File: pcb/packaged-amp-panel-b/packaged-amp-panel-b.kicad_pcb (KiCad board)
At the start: 2 copper layers, 70.9 x 24.2 mm, 0 parts

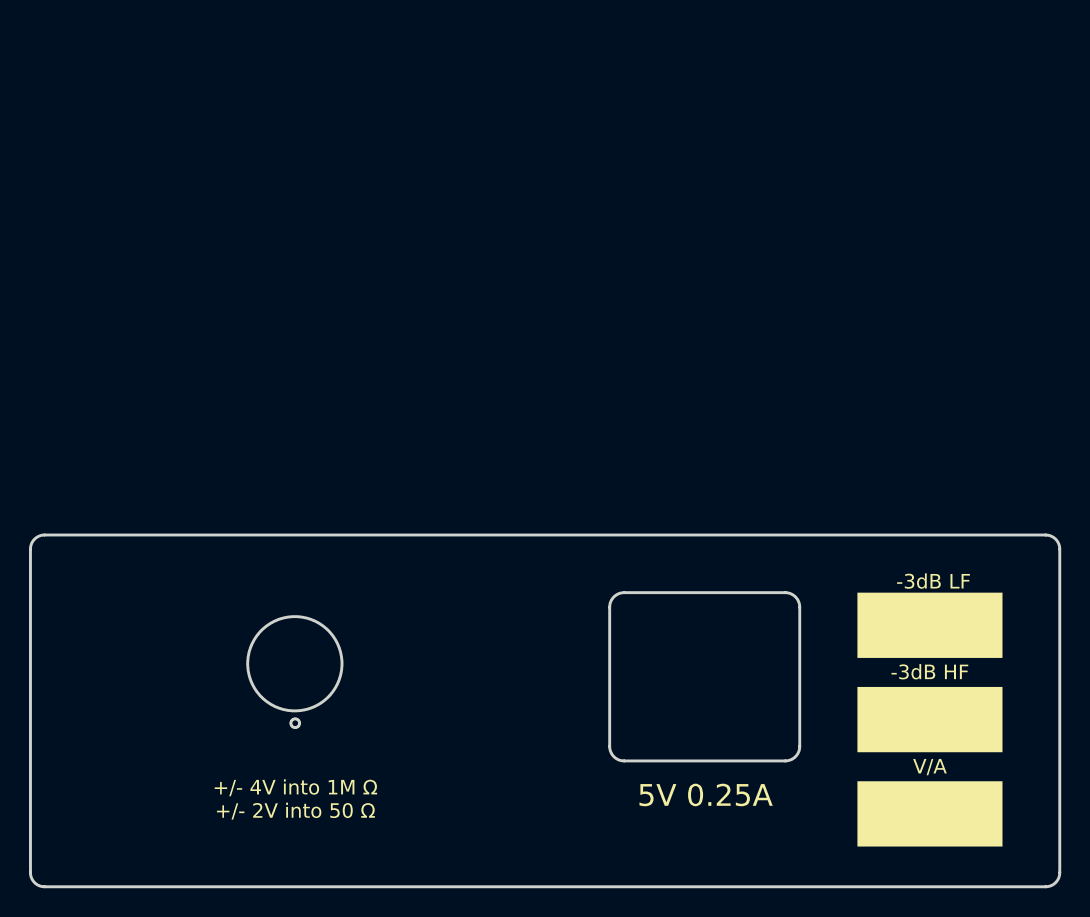
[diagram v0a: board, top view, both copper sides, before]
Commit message: updated panels
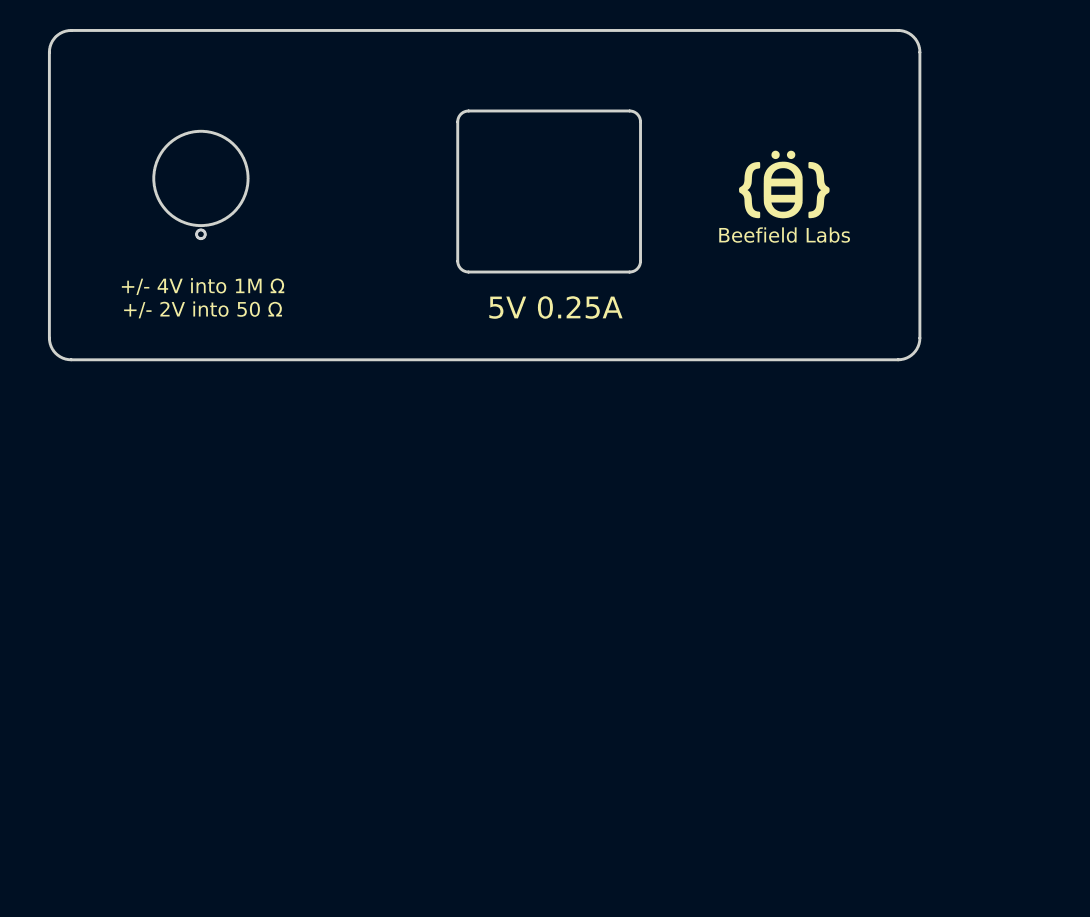
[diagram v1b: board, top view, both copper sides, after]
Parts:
- added G***: LOGO, wbraun_smd:beefield_logo_small, F.Cu at (144.7, 69.8)
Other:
- board size 70.9 x 24.2 mm -> 60 x 22.7 mm
- board text added: "Beefield Labs"
- board text removed: "-3dB HF"
- board text removed: "-3dB LF"
- board text removed: "V/A"

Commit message: next revision
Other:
- outline, holes or cut-outs redrawn
- board text added: "+/- 4V into 1M Ω"
- board text added: "5V 0.4A"
- board text removed: "+/- 4V into 1M Ω +/- 2V into 50 Ω"
- board text removed: "5V 0.25A"
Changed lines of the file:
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@@
   (gr_line (start 152.555626 58.25) (end 95.555626 58.25) (layer "Edge.Cuts") (width 0.2))
   (gr_arc (start 95.555626 80.95) (mid 94.494966 80.51066) (end 94.055626 79.45) (layer "Edge.Cuts") (width 0.2))
-  (gr_line (start 122.95 63.8) (end 134.05 63.8) (layer "Edge.Cuts") (width 0.2))
-  (gr_line (start 134.8 64.55) (end 134.8 74.15) (layer "Edge.Cuts") (width 0.2))
-  (gr_arc (start 122.2 64.55) (mid 122.41967 64.01967) (end 122.95 63.8) (layer "Edge.Cuts") (width 0.2))
+  (gr_line (start 122.95 64.2) (end 134.05 64.2) (layer "Edge.Cuts") (width 0.2))
+  (gr_line (start 134.8 64.95) (end 134.8 74.55) (layer "Edge.Cuts") (width 0.2))
+  (gr_arc (start 122.2 64.95) (mid 122.41967 64.41967) (end 122.95 64.2) (layer "Edge.Cuts") (width 0.2))
   (gr_line (start 95.555626 80.95) (end 152.555626 80.95) (layer "Edge.Cuts") (width 0.2))
   (gr_line (start 94.055626 59.75) (end 94.055626 79.45) (layer "Edge.Cuts") (width 0.2))
-  (gr_line (start 122.2 74.15) (end 122.2 64.55) (layer "Edge.Cuts") (width 0.2))
-  (gr_arc (start 134.05 63.8) (mid 134.580347 64.019661) (end 134.8 64.55) (layer "Edge.Cuts") (width 0.2))
-  (gr_arc (start 134.8 74.15) (mid 134.580329 74.680321) (end 134.05 74.9) (layer "Edge.Cuts") (width 0.2))
+  (gr_line (start 122.2 74.55) (end 122.2 64.95) (layer "Edge.Cuts") (width 0.2))
+  (gr_arc (start 134.05 64.2) (mid 134.58033 64.41967) (end 134.8 64.95) (layer "Edge.Cuts") (width 0.2))
+  (gr_arc (start 134.8 74.55) (mid 134.58033 75.08033) (end 134.05 75.3) (layer "Edge.Cuts") (width 0.2))
   (gr_arc (start 154.055626 79.45) (mid 153.616286 80.51066) (end 152.555626 80.95) (layer "Edge.Cuts") (width 0.2))
-  (gr_arc (start 122.95 74.9) (mid 122.41967 74.68033) (end 122.2 74.15) (layer "Edge.Cuts") (width 0.2))
+  (gr_arc (start 122.95 75.3) (mid 122.41967 75.08033) (end 122.2 74.55) (layer "Edge.Cuts") (width 0.2))
   (gr_arc (start 152.555626 58.25) (mid 153.616286 58.68934) (end 154.055626 59.75) (layer "Edge.Cuts") (width 0.2))
-  (gr_line (start 134.05 74.9) (end 122.95 74.9) (layer "Edge.Cuts") (width 0.2))
+  (gr_line (start 134.05 75.3) (end 122.95 75.3) (layer "Edge.Cuts") (width 0.2))
   (gr_circle (center 104.5 68.45) (end 107.75 68.45) (layer "Edge.Cuts") (width 0.2) (fill none))
   (gr_arc (start 94.055626 59.75) (mid 94.494966 58.68934) (end 95.555626 58.25) (layer "Edge.Cuts") (width 0.2))
@@
     (effects (font (size 1 1) (thickness 0.15)))
   )
-  (gr_text "+/- 4V into 1M Ω\n+/- 2V into 50 Ω" (at 104.6 76.7) (layer "F.SilkS")
+  (gr_text "+/- 4V into 1M Ω\n" (at 104.6 75.75) (layer "F.SilkS")
     (effects (font (size 1 1) (thickness 0.15)))
   )
-  (gr_text "5V 0.25A" (at 128.9 77.4) (layer "F.SilkS")
+  (gr_text "5V 0.4A" (at 128.9 77.4) (layer "F.SilkS")
     (effects (font (size 1.5 1.5) (thickness 0.3)))
   )
   (via (at 104.5 72.3) (size 0.8) (drill 0.4) (layers "F.Cu" "B.Cu") (free) (net 0))
-  (group "" (id f9fdcc45-efb5-407b-b873-9a2d7f0315bf)
-    (members
-      07d800d4-d1db-46ff-ae85-79cface2e4d4
-      0cdfe85b-4f6e-4881-ae9b-b3a882345efb
-      0ddb953f-205f-442b-b848-cf6a84317acc
-      3ecff5c9-24c9-4b4c-91e3-d4a830dd4dd0
-      40e926c5-3a86-445a-9f98-5d4e13723fc0
-      5358da93-8fd2-4dae-9497-ff676879ac9e
-      758d1bd0-f422-43f7-91fd-b4af91de7a5b
-      8144efa2-cec2-46cd-8eab-3e82ee343a28
-      8cc84535-8f6b-4ccb-b4cf-62f6cd0d6d7e
-      97031a12-d7c5-4715-afb1-3668add88d16
-      98678171-d971-4195-bd43-daab671d4ca8
-      9c24e488-9c8d-49b2-9078-ea3751022922
-      a7e9c2fe-3664-4278-9084-35ef16da3316
-      c01e6209-d77a-466c-bdb7-680bf35e795a
-      d7eaec30-a976-4998-a849-895c3e24c2d4
-      f952d511-d473-4134-9274-6869ab0e1b67
-      ff6fc7e0-808d-45fd-aa64-d0c7724f8d98
-    )
-  )
 )
